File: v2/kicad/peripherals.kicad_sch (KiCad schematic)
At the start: 7 parts, among them P2 5k, U1 6526, U11 74ACT245, U2 W65C22SxP

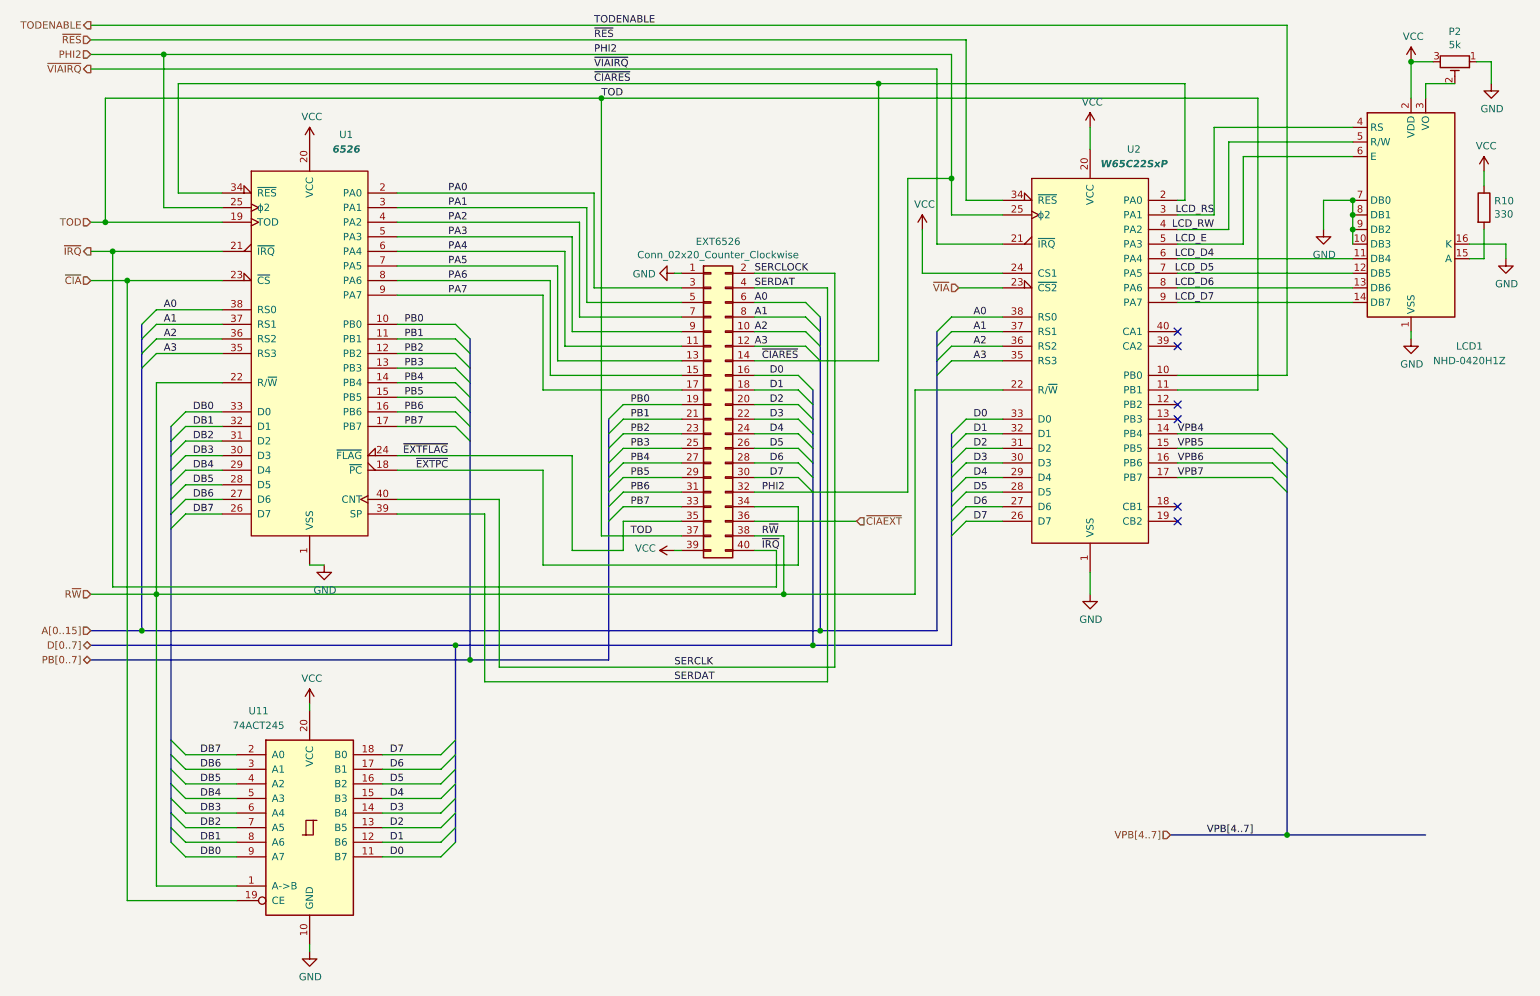
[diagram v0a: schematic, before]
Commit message: PCB Tweaks
Tracks optimized.
SMD components moved to top layer.
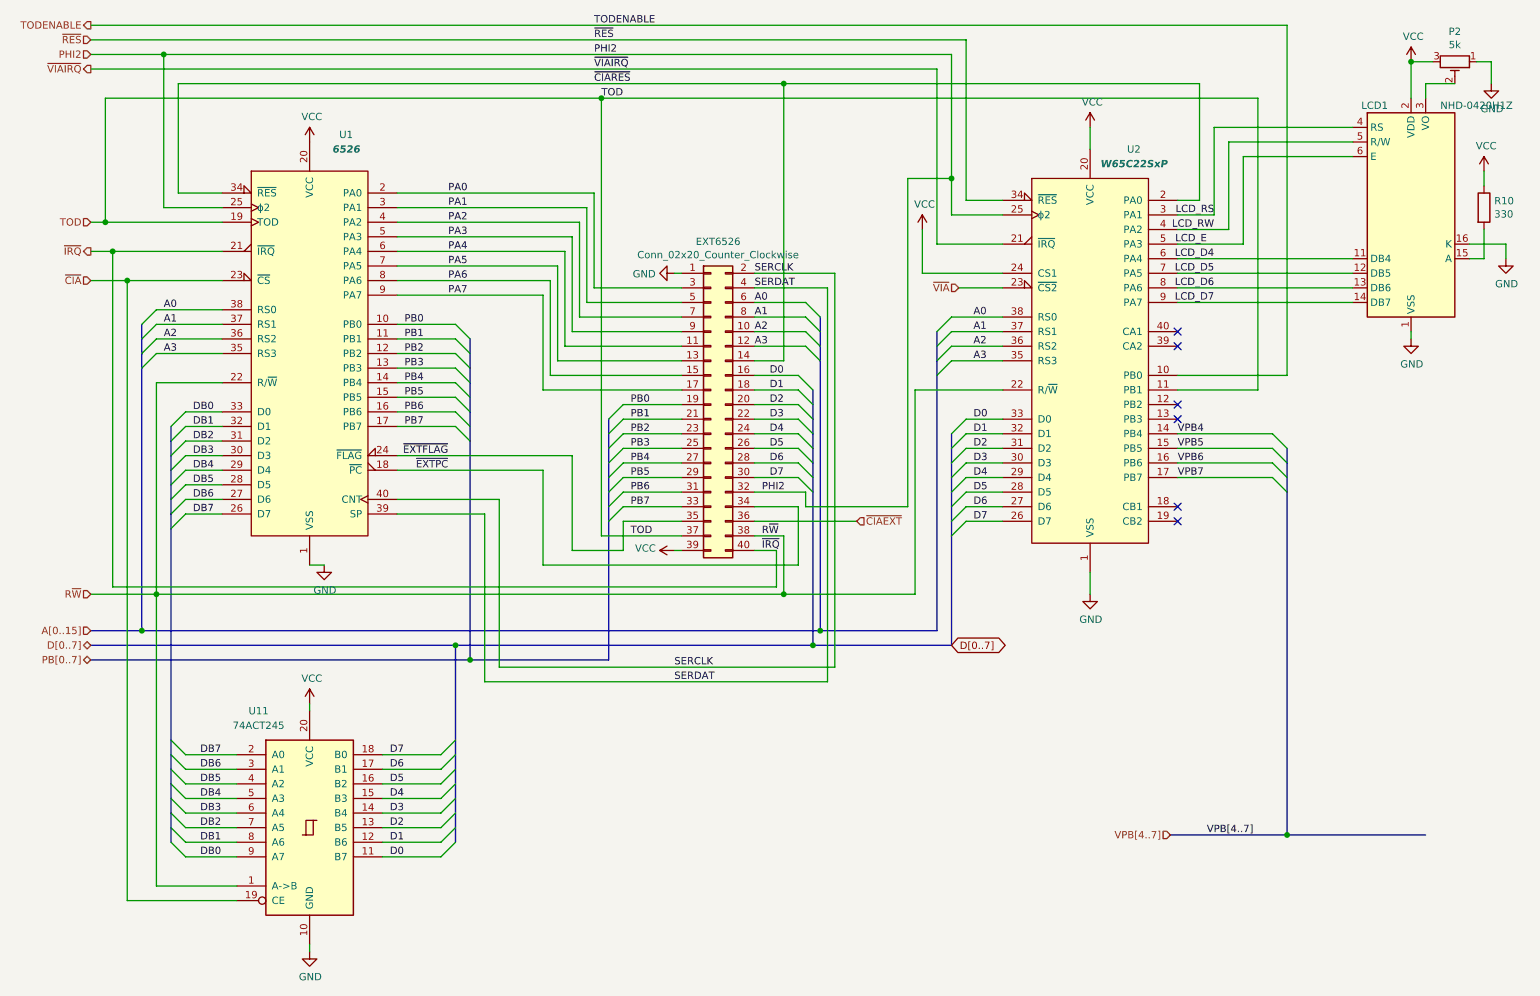
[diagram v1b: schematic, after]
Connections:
- net GND: no longer LCD1.10 (DB3), LCD1.7 (DB0), LCD1.8 (DB1), LCD1.9 (DB2)
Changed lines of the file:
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@@
   (junction (at 48.26 27.94) (diameter 1.016) (color 0 0 0 0))
   (junction (at 124.46 35.56) (diameter 1.016) (color 0 0 0 0))
+  (junction (at 156.21 33.02) (diameter 1.016) (color 0 0 0 0))
   (junction (at 156.21 121.92) (diameter 1.016) (color 0 0 0 0))
-  (junction (at 172.72 33.02) (diameter 1.016) (color 0 0 0 0))
   (junction (at 185.42 49.53) (diameter 1.016) (color 0 0 0 0))
-  (junction (at 255.27 53.34) (diameter 1.016) (color 0 0 0 0))
-  (junction (at 255.27 55.88) (diameter 1.016) (color 0 0 0 0))
-  (junction (at 255.27 58.42) (diameter 1.016) (color 0 0 0 0))
   (junction (at 265.43 29.21) (diameter 1.016) (color 0 0 0 0))
   (junction (at 44.45 128.27) (diameter 1.016) (color 0 0 0 0))
@@
   (junction (at 162.56 128.27) (diameter 1.016) (color 0 0 0 0))
   (junction (at 243.84 163.83) (diameter 1.016) (color 0 0 0 0))
+  (no_connect (at 224.79 78.74))
   (no_connect (at 224.79 88.9))
   (no_connect (at 224.79 91.44))
-  (no_connect (at 224.79 78.74))
+  (no_connect (at 224.79 106.68))
   (no_connect (at 224.79 76.2))
-  (no_connect (at 224.79 106.68))
   (no_connect (at 224.79 109.22))
   (bus_entry (at 46.99 72.39) (size -2.54 2.54)
@@
     (stroke (width 0) (type solid) (color 0 0 0 0))
   )
+  (wire (pts (xy 50.8 33.02) (xy 156.21 33.02))
+    (stroke (width 0) (type solid) (color 0 0 0 0))
+  )
   (wire (pts (xy 50.8 52.07) (xy 50.8 33.02))
     (stroke (width 0) (type solid) (color 0 0 0 0))
@@
     (stroke (width 0) (type solid) (color 0 0 0 0))
   )
-  (wire (pts (xy 151.13 81.28) (xy 162.56 81.28))
+  (wire (pts (xy 151.13 81.28) (xy 156.21 81.28))
     (stroke (width 0) (type solid) (color 0 0 0 0))
   )
@@
     (stroke (width 0) (type solid) (color 0 0 0 0))
   )
-  (wire (pts (xy 151.13 104.14) (xy 161.29 104.14))
+  (wire (pts (xy 151.13 104.14) (xy 160.02 104.14))
     (stroke (width 0) (type solid) (color 0 0 0 0))
   )
@@
     (stroke (width 0) (type solid) (color 0 0 0 0))
   )
+  (wire (pts (xy 156.21 33.02) (xy 228.6 33.02))
+    (stroke (width 0) (type solid) (color 0 0 0 0))
+  )
+  (wire (pts (xy 156.21 81.28) (xy 156.21 33.02))
+    (stroke (width 0) (type solid) (color 0 0 0 0))
+  )
   (wire (pts (xy 156.21 111.76) (xy 151.13 111.76))
     (stroke (width 0) (type solid) (color 0 0 0 0))
@@
     (stroke (width 0) (type solid) (color 0 0 0 0))
   )
-  (wire (pts (xy 161.29 104.14) (xy 177.8 104.14))
-    (stroke (width 0) (type solid) (color 0 0 0 0))
-  )
-  (wire (pts (xy 162.56 81.28) (xy 172.72 81.28))
+  (wire (pts (xy 160.02 104.14) (xy 160.02 106.68))
+    (stroke (width 0) (type solid) (color 0 0 0 0))
+  )
+  (wire (pts (xy 160.02 106.68) (xy 177.8 106.68))
     (stroke (width 0) (type solid) (color 0 0 0 0))
   )
@@
     (stroke (width 0) (type solid) (color 0 0 0 0))
   )
-  (wire (pts (xy 172.72 33.02) (xy 50.8 33.02))
-    (stroke (width 0) (type solid) (color 0 0 0 0))
-  )
-  (wire (pts (xy 172.72 33.02) (xy 226.06 33.02))
-    (stroke (width 0) (type solid) (color 0 0 0 0))
-  )
-  (wire (pts (xy 172.72 81.28) (xy 172.72 33.02))
-    (stroke (width 0) (type solid) (color 0 0 0 0))
-  )
-  (wire (pts (xy 177.8 49.53) (xy 177.8 104.14))
+  (wire (pts (xy 177.8 49.53) (xy 177.8 106.68))
     (stroke (width 0) (type solid) (color 0 0 0 0))
   )
@@
     (stroke (width 0) (type solid) (color 0 0 0 0))
   )
-  (wire (pts (xy 224.79 53.34) (xy 226.06 53.34))
-    (stroke (width 0) (type solid) (color 0 0 0 0))
-  )
   (wire (pts (xy 224.79 55.88) (xy 231.14 55.88))
     (stroke (width 0) (type solid) (color 0 0 0 0))
@@
     (stroke (width 0) (type solid) (color 0 0 0 0))
   )
-  (wire (pts (xy 226.06 53.34) (xy 226.06 33.02))
+  (wire (pts (xy 228.6 33.02) (xy 228.6 53.34))
+    (stroke (width 0) (type solid) (color 0 0 0 0))
+  )
+  (wire (pts (xy 228.6 53.34) (xy 224.79 53.34))
     (stroke (width 0) (type solid) (color 0 0 0 0))
   )
@@
     (stroke (width 0) (type solid) (color 0 0 0 0))
   )
-  (wire (pts (xy 250.19 53.34) (xy 250.19 58.42))
-    (stroke (width 0) (type solid) (color 0 0 0 0))
-  )
   (wire (pts (xy 255.27 43.18) (xy 233.68 43.18))
-    (stroke (width 0) (type solid) (color 0 0 0 0))
-  )
-  (wire (pts (xy 255.27 53.34) (xy 250.19 53.34))
-    (stroke (width 0) (type solid) (color 0 0 0 0))
-  )
-  (wire (pts (xy 255.27 53.34) (xy 255.27 55.88))
-    (stroke (width 0) (type solid) (color 0 0 0 0))
-  )
-  (wire (pts (xy 255.27 55.88) (xy 255.27 58.42))
-    (stroke (width 0) (type solid) (color 0 0 0 0))
-  )
-  (wire (pts (xy 255.27 58.42) (xy 255.27 60.96))
     (stroke (width 0) (type solid) (color 0 0 0 0))
   )
@@
     (effects (font (size 1.27 1.27)) (justify left bottom))
   )
-  (label "SERCLOCK" (at 151.13 66.04 0)
+  (label "SERCLK" (at 151.13 66.04 0)
     (effects (font (size 1.27 1.27)) (justify left bottom))
   )
@@
   )
   (label "A3" (at 151.13 78.74 0)
-    (effects (font (size 1.27 1.27)) (justify left bottom))
-  )
-  (label "~CIARES" (at 152.4 81.28 0)
     (effects (font (size 1.27 1.27)) (justify left bottom))
   )
@@
   (label "LCD_D7" (at 231.14 71.12 180)
     (effects (font (size 1.27 1.27)) (justify right bottom))
+  )
+  (global_label "D[0..7]" (shape bidirectional) (at 185.42 130.81 0)    (property "Intersheet References" "${INTERSHEET_REFS}" (id 0) (at 195.949 130.7306 0)
+      (effects (font (size 1.27 1.27)) (justify left) hide)
+    )
+    (effects (font (size 1.27 1.27)) (justify left))
   )
   (hierarchical_label "TODENABLE" (shape output) (at 35.56 22.86 180)
@@
     )
     (property "Datasheet" "" (id 3) (at 209.55 121.92 0)
-      (effects (font (size 1.27 1.27)) hide)
-    )
-  )
-  (symbol (lib_id "power:GND") (at 250.19 58.42 0) (unit 1)
-    (in_bom yes) (on_board yes)
-    (property "Reference" "#PWR0116" (id 0) (at 250.19 64.77 0)
-      (effects (font (size 1.27 1.27)) hide)
-    )
-    (property "Value" "GND" (id 1) (at 250.317 62.8142 0))
-    (property "Footprint" "" (id 2) (at 250.19 58.42 0)
-      (effects (font (size 1.27 1.27)) hide)
-    )
-    (property "Datasheet" "" (id 3) (at 250.19 58.42 0)
       (effects (font (size 1.27 1.27)) hide)
     )
@@
   (symbol (lib_id "Display_Character:NHD-0420H1Z") (at 265.43 55.88 0) (unit 1)
     (in_bom yes) (on_board yes)
-    (property "Reference" "LCD1" (id 0) (at 275.59 78.74 0))
-    (property "Value" "NHD-0420H1Z" (id 1) (at 275.59 81.28 0))
+    (property "Reference" "LCD1" (id 0) (at 259.08 36.83 0))
+    (property "Value" "NHD-0420H1Z" (id 1) (at 270.51 36.83 0)
+      (effects (font (size 1.27 1.27)) (justify left))
+    )
     (property "Footprint" "sbc6526:HD44780_4x20" (id 2) (at 265.43 78.74 0)
       (effects (font (size 1.27 1.27)) hide)
